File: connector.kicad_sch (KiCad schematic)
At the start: 4 parts, among them J6 Conn_01x90_3Row_Header

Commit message: external loops
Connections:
- net 12V_MR: no longer J6.29 (B29)
- net 12V_RAW: no longer J6.30 (B30)
- net 5V_SENSOR_1: no longer J6.10 (A10), J6.40 (A40)
- net 5V_SENSOR_2: no longer J6.14 (A14), J6.47 (B47)
- net AT1: no longer J6.39 (A39)
- net AT2: no longer J6.46 (B46)
- net AT3: no longer J6.35 (A35)
- net AT4: no longer J6.36 (A36)
- net AV1: no longer J6.11 (A11)
- net AV10: no longer J6.67 (A67)
- net AV11: no longer J6.22 (B22)
- net AV2: no longer J6.15 (A15)
- net AV3: no longer J6.37 (A37)
- net AV4: no longer J6.68 (A68)
- net AV5: no longer J6.70 (A70)
- net AV6: no longer J6.17 (B17)
- net AV7: no longer J6.51 (B51)
- net AV8: no longer J6.65 (A65)
- net AV9: no longer J6.66 (A66)
- net CANH: no longer J6.53 (B53)
- net CANH2: no longer J6.77 (B77)
- net CANL: no longer J6.64 (A64)
- net CANL2: no longer J6.76 (B76)
- net DIGITAL_1: no longer J6.41 (A41)
- net DIGITAL_2: no longer J6.63 (A63)
- net DIGITAL_3: no longer J6.86 (B86)
- net DIGITAL_4: no longer J6.71 (A71)
- net DIGITAL_6: no longer J6.5 (A5)
- net ETB1+: no longer J6.3 (A3)
- net ETB1-: no longer J6.2 (A2)
- net ETB2+: no longer J6.32 (A32)
- net ETB2-: no longer J6.62 (A62)
- net GND: no longer J6.1 (A1), J6.12 (A12), J6.13 (A13), J6.16 (B16), J6.21 (B21), J6.28 (B28), J6.33 (A33), J6.34 (A34), J6.38 (A38), J6.43 (A43), J6.44 (A44), J6.69 (A69), J6.74 (A74), J6.75 (A75), J6.9 (A9)
- net HS1: no longer J6.59 (B59)
- net HS2: no longer J6.60 (B60)
- net HS3: no longer J6.89 (B89)
- net HS4: no longer J6.90 (B90)
- net IGN1: no longer J6.61 (A61)
- net IGN10: no longer J6.55 (B55)
- net IGN11: no longer J6.84 (B84)
- net IGN12: no longer J6.19 (B19)
- net IGN2: no longer J6.31 (A31)
- net IGN3: no longer J6.48 (B48)
- net IGN4: no longer J6.52 (B52)
- net IGN5: no longer J6.56 (B56)
- net IGN6: no longer J6.78 (B78)
- net IGN7: no longer J6.79 (B79)
- net IGN8: no longer J6.49 (B49)
- net IGN9: no longer J6.54 (B54)
- net KNOCK_1: no longer J6.45 (A45)
- net KNOCK_2: no longer J6.8 (A8)
- net LS1: no longer J6.42 (A42)
- net LS10: no longer J6.58 (B58)
- net LS11: no longer J6.80 (B80)
- net LS12: no longer J6.82 (B82)
- net LS13: no longer J6.87 (B87)
- net LS14: no longer J6.88 (B88)
- net LS15: no longer J6.83 (B83)
- net LS16: no longer J6.81 (B81)
- net LS2: no longer J6.20 (B20)
- net LS3: no longer J6.23 (B23)
- net LS4: no longer J6.24 (B24)
- net LS5: no longer J6.25 (B25)
- net LS6: no longer J6.26 (B26)
- net LS7: no longer J6.27 (B27)
- net LS8: no longer J6.50 (B50)
- net LS9: no longer J6.57 (B57)
- net VR1+: no longer J6.72 (A72)
- net VR1-: no longer J6.73 (A73)
- net VR2+: no longer J6.6 (A6)
- net VR2-: no longer J6.7 (A7)
- net 12v_PROT_2: now reaches F2.2
- net 12v_PROT_1: now reaches F1.2
- net A4 renamed off_board/A4
- net B18 renamed off_board/B18
- net B85 renamed off_board/B85
- new net off_board/A1: J6.1 (A1)
- new net off_board/A10: J6.10 (A10)
- new net off_board/A11: J6.11 (A11)
- new net off_board/A12: J6.12 (A12)
- new net off_board/A13: J6.13 (A13)
- new net off_board/A14: J6.14 (A14)
- new net off_board/A15: J6.15 (A15)
- new net off_board/A2: J6.2 (A2)
- new net off_board/A3: J6.3 (A3)
- new net off_board/A31: J6.31 (A31)
- new net off_board/A32: J6.32 (A32)
- new net off_board/A33: J6.33 (A33)
- new net off_board/A34: J6.34 (A34)
- new net off_board/A35: J6.35 (A35)
- new net off_board/A36: J6.36 (A36)
- new net off_board/A37: J6.37 (A37)
- new net off_board/A38: J6.38 (A38)
- new net off_board/A39: J6.39 (A39)
- new net off_board/A40: J6.40 (A40)
- new net off_board/A41: J6.41 (A41)
- new net off_board/A42: J6.42 (A42)
- new net off_board/A43: J6.43 (A43)
- new net off_board/A44: J6.44 (A44)
- new net off_board/A45: J6.45 (A45)
- new net off_board/A5: J6.5 (A5)
- new net off_board/A6: J6.6 (A6)
- new net off_board/A61: J6.61 (A61)
- new net off_board/A62: J6.62 (A62)
- new net off_board/A63: J6.63 (A63)
- new net off_board/A64: J6.64 (A64)
- new net off_board/A65: J6.65 (A65)
- new net off_board/A66: J6.66 (A66)
- new net off_board/A67: J6.67 (A67)
- new net off_board/A68: J6.68 (A68)
- new net off_board/A69: J6.69 (A69)
- new net off_board/A7: J6.7 (A7)
- new net off_board/A70: J6.70 (A70)
- new net off_board/A71: J6.71 (A71)
- new net off_board/A72: J6.72 (A72)
- new net off_board/A73: J6.73 (A73)
- new net off_board/A74: J6.74 (A74)
- new net off_board/A75: J6.75 (A75)
- new net off_board/A8: J6.8 (A8)
- new net off_board/A9: J6.9 (A9)
- new net off_board/B16: J6.16 (B16)
- new net off_board/B17: J6.17 (B17)
- new net off_board/B19: J6.19 (B19)
- new net off_board/B20: J6.20 (B20)
- new net off_board/B21: J6.21 (B21)
- new net off_board/B22: J6.22 (B22)
- new net off_board/B23: J6.23 (B23)
- new net off_board/B24: J6.24 (B24)
- new net off_board/B25: J6.25 (B25)
- new net off_board/B26: J6.26 (B26)
- new net off_board/B27: J6.27 (B27)
- new net off_board/B28: J6.28 (B28)
- new net off_board/B29: J6.29 (B29)
- new net off_board/B30: J6.30 (B30)
- new net off_board/B46: J6.46 (B46)
- new net off_board/B47: J6.47 (B47)
- new net off_board/B48: J6.48 (B48)
- new net off_board/B49: J6.49 (B49)
- new net off_board/B50: J6.50 (B50)
- new net off_board/B51: J6.51 (B51)
- new net off_board/B52: J6.52 (B52)
- new net off_board/B53: J6.53 (B53)
- new net off_board/B54: J6.54 (B54)
- new net off_board/B55: J6.55 (B55)
- new net off_board/B56: J6.56 (B56)
- new net off_board/B57: J6.57 (B57)
- new net off_board/B58: J6.58 (B58)
- new net off_board/B59: J6.59 (B59)
- new net off_board/B60: J6.60 (B60)
- new net off_board/B76: J6.76 (B76)
- new net off_board/B77: J6.77 (B77)
- new net off_board/B78: J6.78 (B78)
- new net off_board/B79: J6.79 (B79)
- new net off_board/B80: J6.80 (B80)
- new net off_board/B81: J6.81 (B81)
- new net off_board/B82: J6.82 (B82)
- new net off_board/B83: J6.83 (B83)
- new net off_board/B84: J6.84 (B84)
- new net off_board/B86: J6.86 (B86)
- new net off_board/B87: J6.87 (B87)
- new net off_board/B88: J6.88 (B88)
- new net off_board/B89: J6.89 (B89)
- new net off_board/B90: J6.90 (B90)
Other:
- moved on the sheet: J6A

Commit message: external loops arrangments
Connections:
- net off_board/A1 is gone; now on net GND: J6.1 (A1)
- net off_board/A2 is gone; now on net ETB1-: J6.2 (A2)
- net off_board/A3 is gone; now on net ETB1+: J6.3 (A3)
- net off_board/A4 renamed D_IN_1
- net off_board/A5 renamed D_IN_2
- net off_board/A6 renamed VR_2+
- net off_board/A7 renamed VR_2-
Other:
- moved on the sheet: F1, F2, J6A, J6B

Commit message: external loops arrangments1
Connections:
- net off_board/A8 is gone; now on net AIN_V11: J6.8 (A8)
- net off_board/A9 is gone; now on net GND: J6.9 (A9)

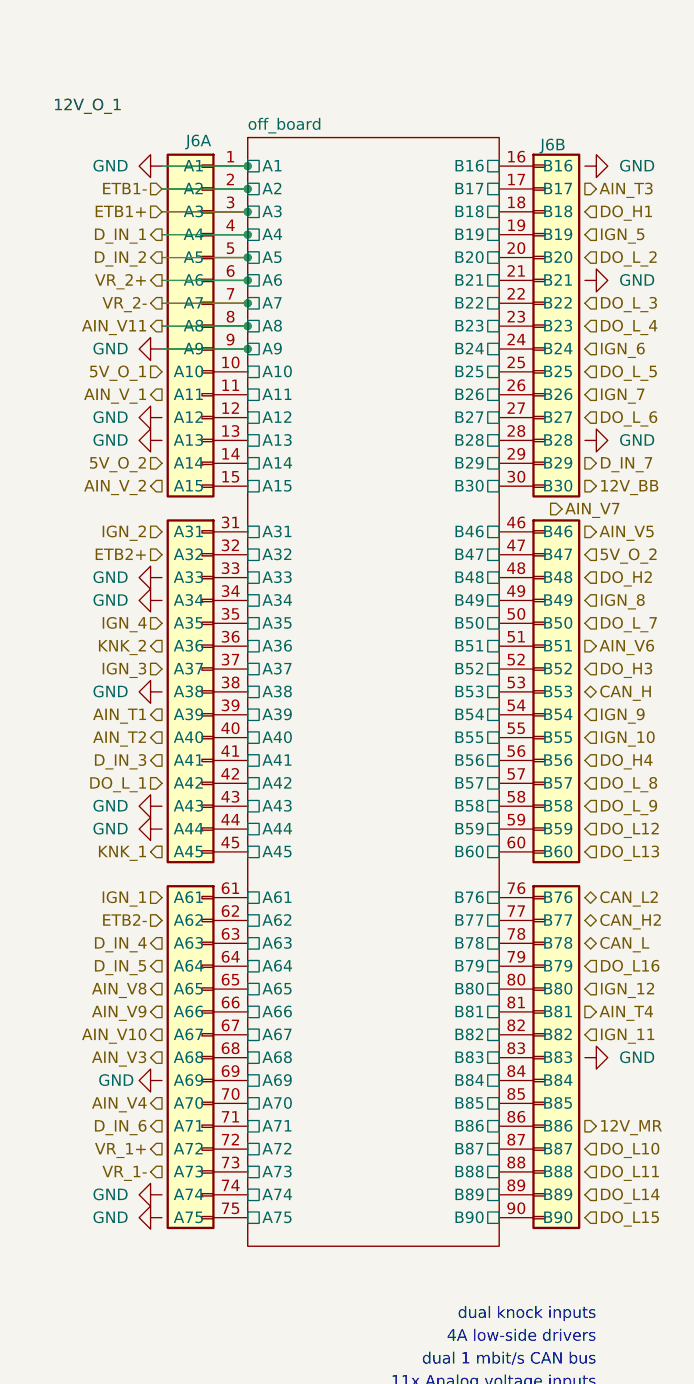
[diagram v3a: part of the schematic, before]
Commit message: air conditioner updated
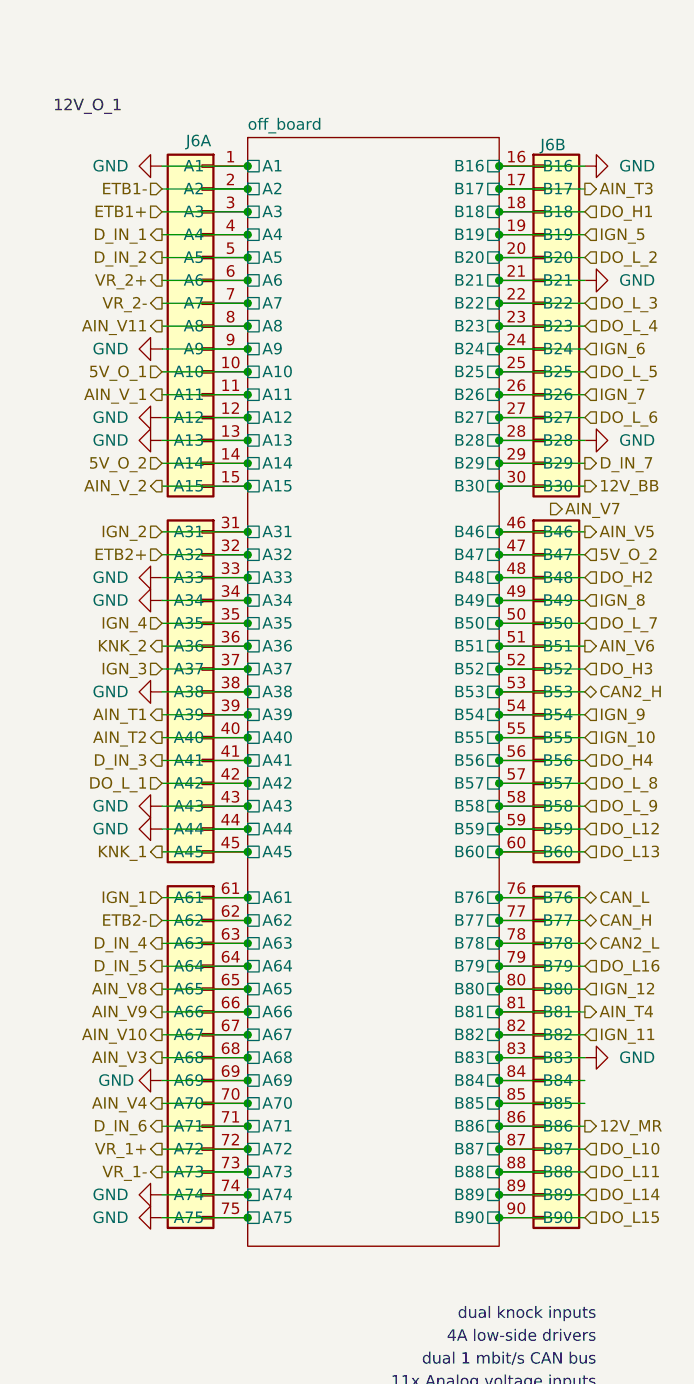
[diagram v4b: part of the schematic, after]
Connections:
- net off_board/A10 is gone; now on net 5V_O_1: J6.10 (A10)
- net off_board/A11 is gone; now on net AIN_V_1: J6.11 (A11)
- net off_board/A12 is gone; now on net GND: J6.12 (A12)
- net off_board/A13 is gone; now on net GND: J6.13 (A13)
- net off_board/A14 is gone; now on net 5V_O_2: J6.14 (A14)
- net off_board/A15 is gone; now on net AIN_V_2: J6.15 (A15)
- net off_board/A31 is gone; now on net IGN_2: J6.31 (A31)
- net off_board/A32 is gone; now on net ETB2+: J6.32 (A32)
- net off_board/A33 is gone; now on net GND: J6.33 (A33)
- net off_board/A34 is gone; now on net GND: J6.34 (A34)
- net off_board/A35 is gone; now on net IGN_4: J6.35 (A35)
- net off_board/A36 is gone; now on net KNK_2: J6.36 (A36)
- net off_board/A37 is gone; now on net IGN_3: J6.37 (A37)
- net off_board/A38 is gone; now on net GND: J6.38 (A38)
- net off_board/A39 is gone; now on net AIN_T1: J6.39 (A39)
- net off_board/A40 is gone; now on net AIN_T2: J6.40 (A40)
- net off_board/A41 is gone; now on net D_IN_3: J6.41 (A41)
- net off_board/A42 is gone; now on net DO_L_1: J6.42 (A42)
- net off_board/A43 is gone; now on net GND: J6.43 (A43)
- net off_board/A44 is gone; now on net GND: J6.44 (A44)
- net off_board/A45 is gone; now on net KNK_1: J6.45 (A45)
- net off_board/A61 is gone; now on net IGN_1: J6.61 (A61)
- net off_board/A62 is gone; now on net ETB2-: J6.62 (A62)
- net off_board/A63 is gone; now on net D_IN_4: J6.63 (A63)
- net off_board/A64 is gone; now on net D_IN_5: J6.64 (A64)
- net off_board/A65 is gone; now on net AIN_V8: J6.65 (A65)
- net off_board/A66 is gone; now on net AIN_V9: J6.66 (A66)
- net off_board/A67 is gone; now on net AIN_V10: J6.67 (A67)
- net off_board/A68 is gone; now on net AIN_V3: J6.68 (A68)
- net off_board/A69 is gone; now on net GND: J6.69 (A69)
- net off_board/A70 is gone; now on net AIN_V4: J6.70 (A70)
- net off_board/A71 is gone; now on net D_IN_6: J6.71 (A71)
- net off_board/A72 is gone; now on net VR_1+: J6.72 (A72)
- net off_board/A73 is gone; now on net VR_1-: J6.73 (A73)
- net off_board/A74 is gone; now on net GND: J6.74 (A74)
- net off_board/A75 is gone; now on net GND: J6.75 (A75)
- net off_board/B16 is gone; now on net GND: J6.16 (B16)
- net off_board/B17 is gone; now on net AIN_T3: J6.17 (B17)
- net off_board/B18 is gone; now on net DO_H1: J6.18 (B18)
- net off_board/B19 is gone; now on net IGN_5: J6.19 (B19)
- net off_board/B20 is gone; now on net DO_L_2: J6.20 (B20)
- net off_board/B21 is gone; now on net GND: J6.21 (B21)
- net off_board/B22 is gone; now on net DO_L_3: J6.22 (B22)
- net off_board/B23 is gone; now on net DO_L_4: J6.23 (B23)
- net off_board/B24 is gone; now on net IGN_6: J6.24 (B24)
- net off_board/B25 is gone; now on net DO_L_5: J6.25 (B25)
- net off_board/B26 is gone; now on net IGN_7: J6.26 (B26)
- net off_board/B27 is gone; now on net DO_L_6: J6.27 (B27)
- net off_board/B28 is gone; now on net GND: J6.28 (B28)
- net off_board/B29 is gone; now on net D_IN_7: J6.29 (B29)
- net off_board/B30 is gone; now on net 12V_BB: J6.30 (B30)
- net off_board/B46 is gone; now on net AIN_V5: J6.46 (B46)
- net off_board/B47 is gone; now on net 5V_O_2: J6.47 (B47)
- net off_board/B48 is gone; now on net DO_H2: J6.48 (B48)
- net off_board/B49 is gone; now on net IGN_8: J6.49 (B49)
- net off_board/B50 is gone; now on net DO_L_7: J6.50 (B50)
- net off_board/B51 is gone; now on net AIN_V6: J6.51 (B51)
- net off_board/B52 is gone; now on net DO_H3: J6.52 (B52)
- net off_board/B54 is gone; now on net IGN_9: J6.54 (B54)
- net off_board/B55 is gone; now on net IGN_10: J6.55 (B55)
- net off_board/B56 is gone; now on net DO_H4: J6.56 (B56)
- net off_board/B57 is gone; now on net DO_L_8: J6.57 (B57)
- net off_board/B58 is gone; now on net DO_L_9: J6.58 (B58)
- net off_board/B59 is gone; now on net DO_L12: J6.59 (B59)
- net off_board/B60 is gone; now on net DO_L13: J6.60 (B60)
- net off_board/B76 is gone; now on net CAN_L: J6.76 (B76)
- net off_board/B77 is gone; now on net CAN_H: J6.77 (B77)
- net off_board/B79 is gone; now on net DO_L16: J6.79 (B79)
- net off_board/B80 is gone; now on net IGN_12: J6.80 (B80)
- net off_board/B81 is gone; now on net AIN_T4: J6.81 (B81)
- net off_board/B82 is gone; now on net IGN_11: J6.82 (B82)
- net off_board/B83 is gone; now on net GND: J6.83 (B83)
- net off_board/B86 is gone; now on net 12V_MR: J6.86 (B86)
- net off_board/B87 is gone; now on net DO_L10: J6.87 (B87)
- net off_board/B88 is gone; now on net DO_L11: J6.88 (B88)
- net off_board/B89 is gone; now on net DO_L14: J6.89 (B89)
- net off_board/B90 is gone; now on net DO_L15: J6.90 (B90)
- net off_board/B53 renamed CAN2_H
- net off_board/B78 renamed CAN2_L
